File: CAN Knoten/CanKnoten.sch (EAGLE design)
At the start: 41 parts, among them IC1 74LS165D, IC2 74LS165D, K1 68711614522, K2 68711614522, K3 68711614522, K4 68711614522, Q1 HC49-U - 16MHz, Q2 HC49-U - xMHz

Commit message: 
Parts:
- removed IC2: 74LS165D, 74xx-us:74LS165D
- removed RN1: (no value), resistor-array:745-10
- removed S2: 219-08, switch-dil:219-08
- added PAD1, PAD2: (no value), wirepad:SMD5
- added X1: MSTBV3, con-phoenix-508:MSTBV3
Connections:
- net N$31 renamed PDI_RESET
- net N$33 renamed REAR_MCP2515_TXCAN
- net N$34 renamed REAR_MCP2515_RXCAN
- removed net 74XX165_SH/LD_IC2: D1.(ADC10)PB2, IC2A.SH/!LD
- removed net CAN_BITRATE_0: IC2A.A, K4.3
- removed net CAN_BITRATE_1: IC2A.B, K4.4
- removed net CAN_BITRATE_2: IC2A.C, K4.5
- removed net CAN_BITRATE_3: IC2A.D, K4.6
- removed net CAN_BITRATE_4: IC2A.E, K4.7
- removed net CAN_BITRATE_5: IC2A.F, K4.8
- removed net CAN_BITRATE_6: IC2A.G, K4.9
- removed net CAN_BITRATE_7: IC2A.H, K4.10
- removed net N$13: D1.(AREF/AC0/ADC0)PA0
- removed net N$14: D1.(AC1/ADC1)PA1
- removed net N$18: D1.(AC2/ADC2)PA2
- removed net N$19: K3.9, RN1.8, S2.10
- removed net N$2: IC1A.QH, IC2A.SER
- removed net N$20: D1.(SDA/OC0A)PE0
- removed net N$21: D1.(SCL/OC0B)PE1
- removed net N$30: K3.10, RN1.9, S2.9
- removed net N$4: K3.3, RN1.1, S2.16
- removed net N$5: K3.4, RN1.2, S2.15
- removed net N$6: K3.5, RN1.3, S2.14
- removed net N$7: K3.6, RN1.4, S2.13
- removed net N$8: K3.7, RN1.6, S2.12
- removed net N$9: K3.8, RN1.7, S2.11
- new net REAR_CANH: K3.12, X1-1.1
- new net REAR_CANL: K3.11, X1-3.1
- net 74XX165_CLK: no longer IC2A.CLK
- net 74XX165_OUT: now also IC1A.QH; no longer IC2A.QH
- net FRONT_GND: now also PAD1.P
- net FRONT_VCC: now also PAD2.P
- net GND: now also IC1A.SER; no longer IC2A.INH, IC2P.GND
- net MCP2515_INT: now also D1.(OC0D)PE3; no longer D1.(AC3/ADC3)PA3
- net MCP2515_RXCAN: now also D1.(OC0C)PE2; no longer D1.(AC4/ADC4)PA4
- net REAR_GND: now also X1-2.1; no longer S2.1, S2.2, S2.3, S2.4, S2.5, S2.6, S2.7, S2.8
- net REAR_VCC: now also K3.3; no longer K3.11, K3.12, RN1.10, RN1.5
- net VCC: now also K4.3; no longer IC2P.VCC, K4.11, K4.12

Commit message: 
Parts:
- added XB1: (no value), Wannenstiftleisten:WSL10
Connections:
- removed net N$17: C6.2, C7.2
- new net EXTENDED_I2C_SCL: D1.(SCL/XCK0/OC0AHS/OC0B)PC1, K4.7
- new net EXTENDED_I2C_SDA: D1.(SDA/OC0ALS/OC0A)PC0, K4.6
- new net EXTENDED_SPI_MISO: D1.(MISO/OC0DLS)PC6, K4.8
- new net EXTENDED_SPI_MOSI: D1.(MOSI/OC1B/OC0CHS)PC5, K4.9
- new net EXTENDED_SPI_SCK: D1.(EVOUT/CLKOUT/SCK/OC0DHS)PC7, K4.10
- new net EXTENDED_UART_RXD: D1.(RXD0/OC0BLS/OC0C)PC2, K4.4
- new net EXTENDED_UART_TXD: D1.(TXD0/OC0BHS/OC0D)PC3, K4.5
- new net N$2: K3.4, XB1.1..1
- new net N$4: K3.5, XB1.2..1
- new net N$5: K3.6, XB1.3..1
- new net N$6: K3.7, XB1.4..1
- new net N$7: K3.8, XB1.5..1
- new net N$8: K3.9, XB1.6..1
- new net N$9: K3.10, XB1.7..1
- net GND: now also C6.2, C7.2
- net MCP2551_CANH: now also K4.12
- net MCP2551_CANL: now also K4.11
- net REAR_GND: now also XB1.8..1
- net REAR_VCC: now also XB1.10..1, XB1.9..1

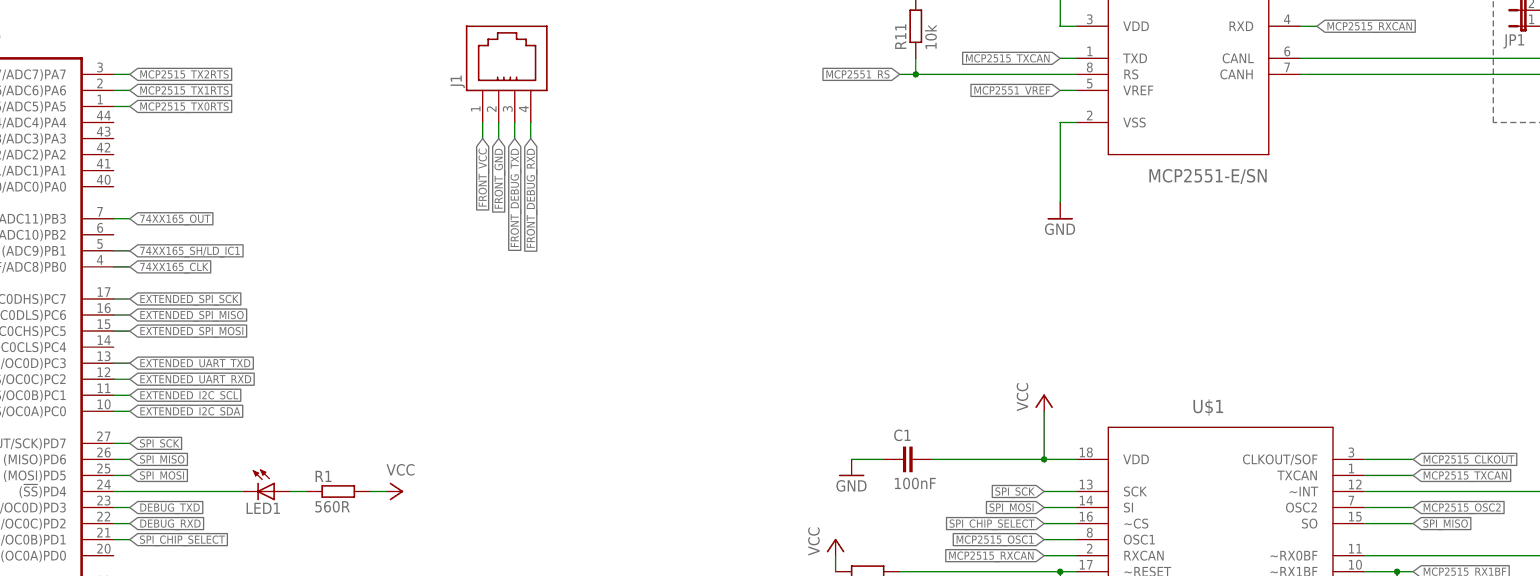
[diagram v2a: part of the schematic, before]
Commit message: 
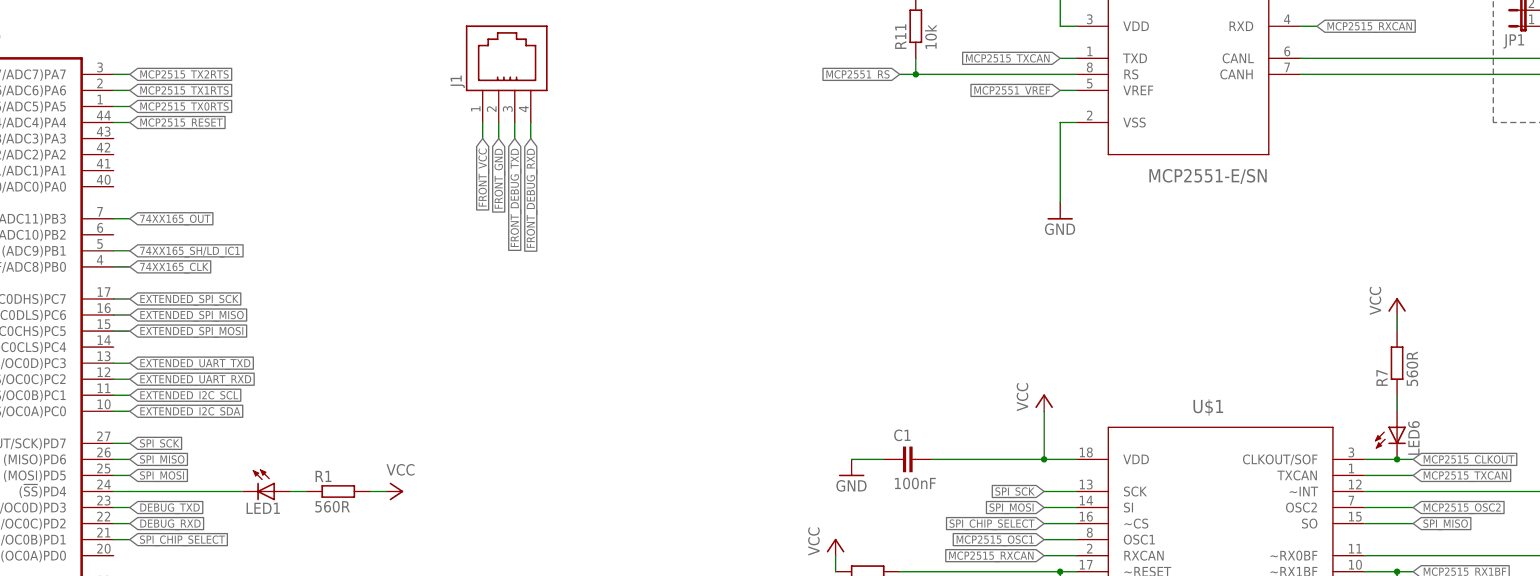
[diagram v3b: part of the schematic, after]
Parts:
- added LED6: (no value), led:LEDSML1206
- added R7: 560R, rcl:R-EU_R1206
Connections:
- new net N$13: LED6.A, R7.1
- net MCP2515_CLKOUT: now also LED6.C
- net MCP2515_RESET: now also D1.(AC4/ADC4)PA4
- net VCC: now also R7.2
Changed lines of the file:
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@@
 <part name="XB1" library="Wannenstiftleisten" deviceset="WSL10" device=""/>
 <part name="GND9" library="supply1" deviceset="GND" device=""/>
+<part name="LED6" library="led" deviceset="LED" device="SML1206"/>
+<part name="R7" library="rcl" deviceset="R-EU_" device="R1206" value="560R"/>
+<part name="P+11" library="supply1" deviceset="VCC" device=""/>
 </parts>
 <sheets>
@@
 <instance part="XB1" gate=".10" x="-190.5" y="-170.18"/>
 <instance part="GND9" gate="1" x="-220.98" y="78.74"/>
+<instance part="LED6" gate="G$1" x="73.66" y="63.5"/>
+<instance part="R7" gate="G$1" x="73.66" y="73.66" rot="R90"/>
+<instance part="P+11" gate="VCC" x="73.66" y="83.82"/>
 </instances>
 <busses>
@@
 <pinref part="P+5" gate="VCC" pin="VCC"/>
 </segment>
+<segment>
+<pinref part="R7" gate="G$1" pin="2"/>
+<pinref part="P+11" gate="VCC" pin="VCC"/>
+<wire x1="73.66" y1="81.28" x2="73.66" y2="78.74" width="0.1524" layer="91"/>
+</segment>
 </net>
 <net name="GND" class="0">
@@
 <junction x="20.32" y="40.64"/>
 </segment>
+<segment>
+<pinref part="D1" gate="G$1" pin="(AC4/ADC4)PA4"/>
+<wire x1="-129.54" y1="111.76" x2="-127" y2="111.76" width="0.1524" layer="91"/>
+<label x="-127" y="111.76" size="1.27" layer="95" xref="yes"/>
+</segment>
 </net>
 <net name="MCP2515_RXCAN" class="0">
@@
 <label x="76.2" y="58.42" size="1.27" layer="95" xref="yes"/>
 <wire x1="73.66" y1="58.42" x2="76.2" y2="58.42" width="0.1524" layer="91"/>
+<pinref part="LED6" gate="G$1" pin="C"/>
+<junction x="73.66" y="58.42"/>
 </segment>
 </net>
@@
 </segment>
 </net>
+<net name="N$13" class="0">
+<segment>
+<pinref part="LED6" gate="G$1" pin="A"/>
+<pinref part="R7" gate="G$1" pin="1"/>
+<wire x1="73.66" y1="68.58" x2="73.66" y2="66.04" width="0.1524" layer="91"/>
+</segment>
+</net>

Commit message: 
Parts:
- added LED7, LED8, LED9: (no value), led:LEDSML1206
- added R10, R13, R9: 560R, rcl:R-EU_R1206
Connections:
- new net N$14: LED7.A, R9.1
- new net N$17: LED8.A, R10.1
- new net N$18: LED9.A, R13.1
- net MCP2515_TX0RTS: now also LED7.C
- net MCP2515_TX1RTS: now also LED8.C
- net MCP2515_TX2RTS: now also LED9.C
- net VCC: now also R10.2, R13.2, R9.2
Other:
- moved on the sheet: C1, C2, C3, C4, C5, C6, C7, D1, IC1, IC1P, J1, JP1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

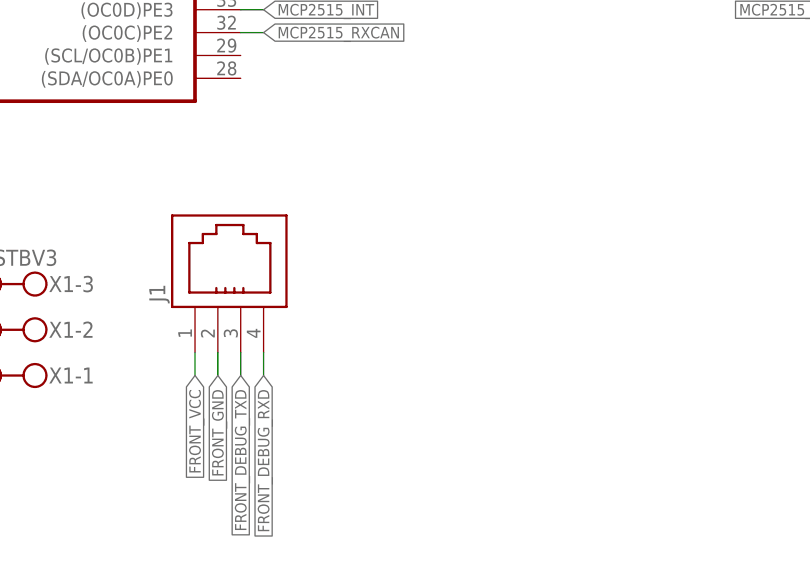
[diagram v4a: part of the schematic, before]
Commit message: 
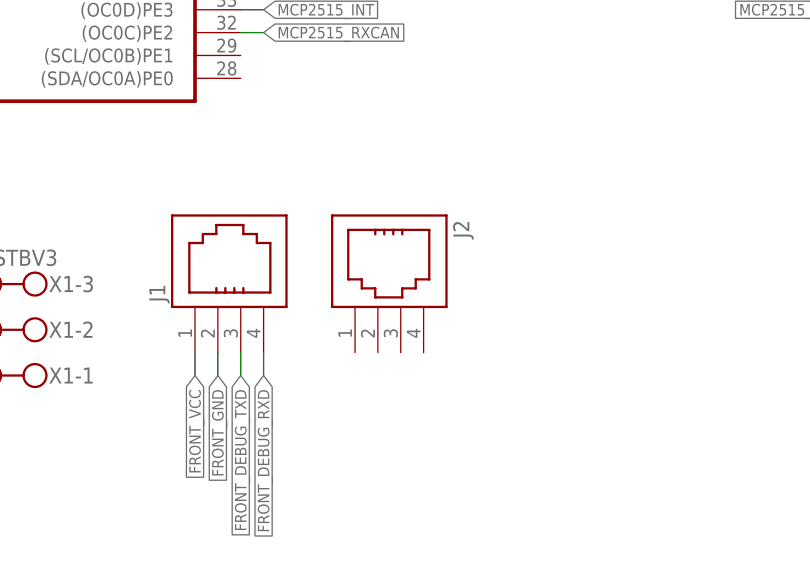
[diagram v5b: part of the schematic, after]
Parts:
- added J2: (no value), InputOutputIO (rev18b):615004144021
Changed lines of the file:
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@@
 <part name="P+18" library="supply1" deviceset="VCC" device=""/>
 <part name="U$5" library="!!!Hesch Automation Frame!!!" deviceset="HESCH(C)DINA3" device=""/>
+<part name="J2" library="InputOutputIO (rev18b)" deviceset="615004144021" device=""/>
 </parts>
 <sheets>
@@
 <instance part="P+18" gate="VCC" x="180.34" y="165.1"/>
 <instance part="U$5" gate="G$1" x="0" y="0"/>
+<instance part="J2" gate="G$1" x="124.46" y="111.76" rot="R270"/>
 </instances>
 <busses>
